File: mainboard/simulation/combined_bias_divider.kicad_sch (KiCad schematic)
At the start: 23 parts

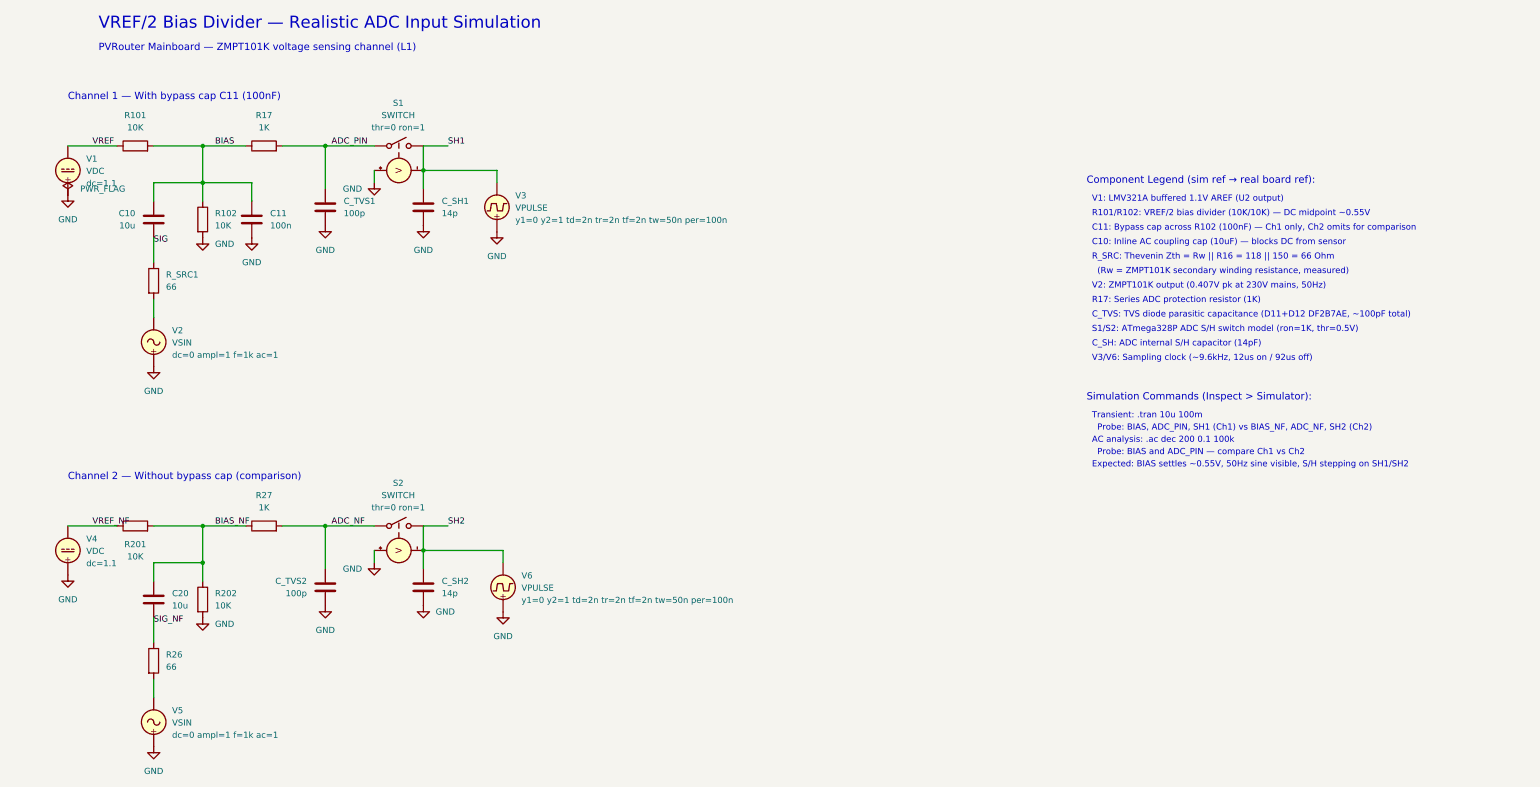
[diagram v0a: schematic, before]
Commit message: Add LCSC part numbers, MPC10-5 footprint, and simulation updates
- Add LCSC fields to mk2Wifi schematic (20 components for JLCPCB assembly)
- Add LCSC fields to mainboard schematic (18x 20K resistors, 12x 100nF caps)
- Add power indicator LED (LED40) and series resistor (R43) to mainboard
- Add MPC10-5 AC-DC converter custom footprint and TMF_05105 3D model
- Add CT and combined bias divider simulation schematics with generators
- Update mainboard PCB layout and bias divider simulation

Co-Authored-By: Claude Opus 4.6 <noreply@anthropic.com>
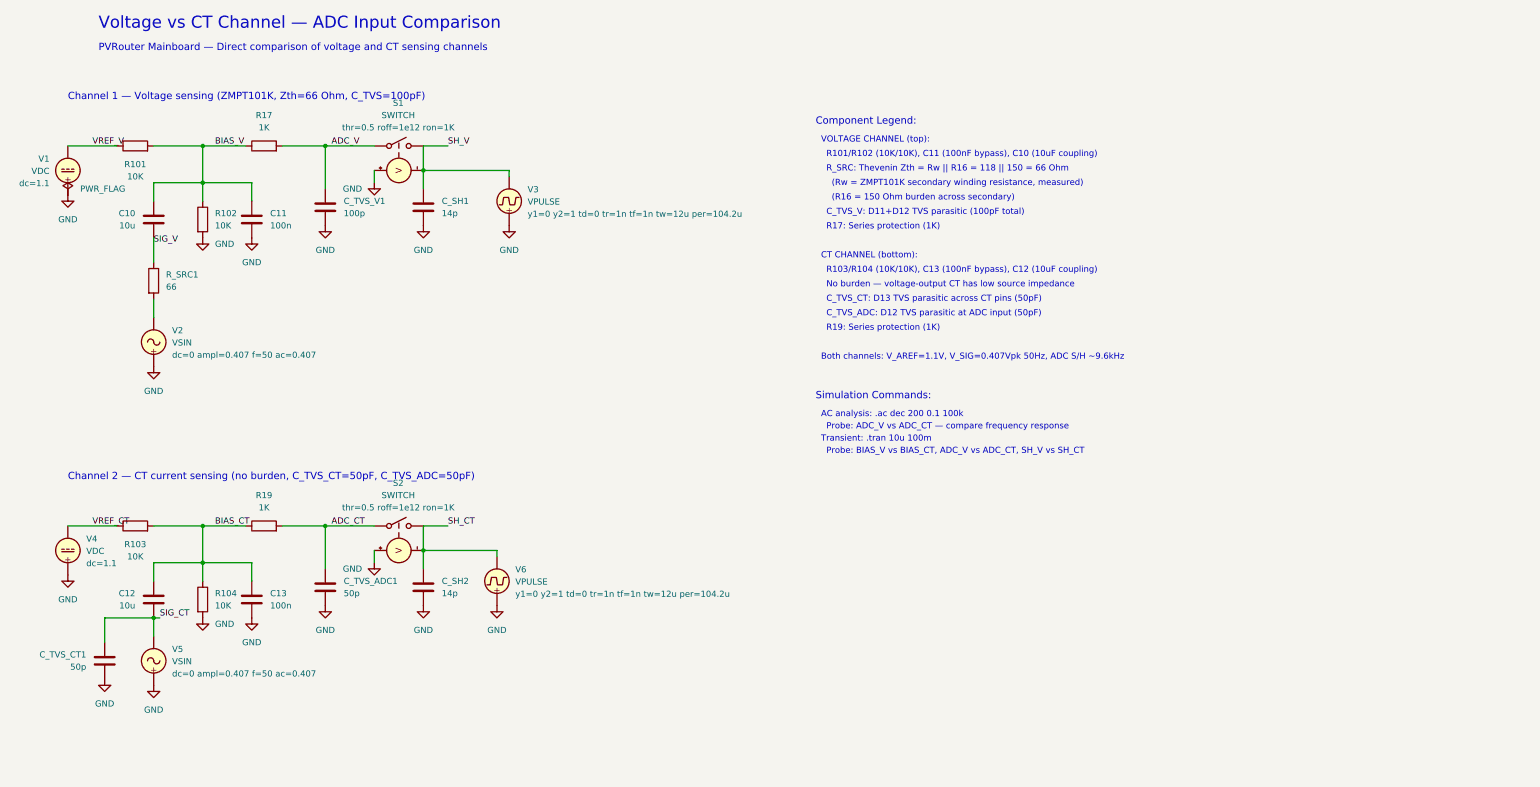
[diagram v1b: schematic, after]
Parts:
- removed C20: 10u, symbol Device:C
- removed C_TVS1, C_TVS2: 100p, symbol Device:C
- removed R201, R202: 10K, symbol Device:R
- removed R26: 66, symbol Device:R
- removed R27: 1K, symbol Device:R
- added C12: 10u, symbol Device:C
- added C13: 100n, symbol Device:C
- added C_TVS_ADC1, C_TVS_CT1: 50p, symbol Device:C
- added C_TVS_V1: 100p, symbol Device:C
- added R103, R104: 10K, symbol Device:R
- added R19: 1K, symbol Device:R
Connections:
- net GND: now also C13.2, C_TVS_ADC1.2, C_TVS_CT1.2, C_TVS_V1.2, R104.2
- net SIG_CT: now reaches V5.2
- net SIG_CT: now also C12.2, C_TVS_CT1.1
- net ADC_NF renamed ADC_CT
- net ADC_CT: now also C_TVS_ADC1.1, R19.2
- net ADC_PIN renamed ADC_V
- net ADC_V: now also C_TVS_V1.1
- net BIAS renamed BIAS_V
- net SH1 renamed SH_V
- net SH2 renamed SH_CT
- net SIG renamed SIG_V
- net VREF renamed VREF_V
- net VREF_NF renamed VREF_CT
- net VREF_CT: now also R103.1
- new net BIAS_CT: C12.1, C13.1, R103.2, R104.1, R19.1
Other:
- note added: "(R16 = 150 Ohm burden across secondary)"
- note added: "Both channels: V_AREF=1.1V, V_SIG=0.407Vpk 50Hz, ADC S/H ~9.6kHz"
- note added: "CT CHANNEL (bottom):"
- note added: "C_TVS_ADC: D12 TVS parasitic at ADC input (50pF)"
- note added: "C_TVS_CT: D13 TVS parasitic across CT pins (50pF)"
- note added: "C_TVS_V: D11+D12 TVS parasitic (100pF total)"
- note added: "Channel 1 — Voltage sensing (ZMPT101K, Zth=66 Ohm, C_TVS=100pF)"
- note added: "Channel 2 — CT current sensing (no burden, C_TVS_CT=50pF, C_TVS_ADC=50pF)"
- note added: "Component Legend:"
- note added: "No burden — voltage-output CT has low source impedance"
- note added: "PVRouter Mainboard — Direct comparison of voltage and CT sensing channels"
- note added: "Probe: ADC_V vs ADC_CT — compare frequency response"
- note added: "Probe: BIAS_V vs BIAS_CT, ADC_V vs ADC_CT, SH_V vs SH_CT"
- note added: "R101/R102 (10K/10K), C11 (100nF bypass), C10 (10uF coupling)"
- note added: "R103/R104 (10K/10K), C13 (100nF bypass), C12 (10uF coupling)"
- note added: "R17: Series protection (1K)"
- note added: "R19: Series protection (1K)"
- note added: "Simulation Commands:"
- note added: "VOLTAGE CHANNEL (top):"
- note added: "Voltage vs CT Channel — ADC Input Comparison"
- note removed: "C10: Inline AC coupling cap (10uF) — blocks DC from sensor"
- note removed: "C11: Bypass cap across R102 (100nF) — Ch1 only, Ch2 omits for comparison"
- note removed: "C_SH: ADC internal S/H capacitor (14pF)"
- note removed: "C_TVS: TVS diode parasitic capacitance (D11+D12 DF2B7AE, ~100pF total)"
- note removed: "Channel 1 — With bypass cap C11 (100nF)"
- note removed: "Channel 2 — Without bypass cap (comparison)"
- note removed: "Component Legend (sim ref → real board ref):"
- note removed: "Expected: BIAS settles ~0.55V, 50Hz sine visible, S/H stepping on SH1/SH2"
- note removed: "PVRouter Mainboard — ZMPT101K voltage sensing channel (L1)"
- note removed: "Probe: BIAS and ADC_PIN — compare Ch1 vs Ch2"
- note removed: "Probe: BIAS, ADC_PIN, SH1 (Ch1) vs BIAS_NF, ADC_NF, SH2 (Ch2)"
- note removed: "R101/R102: VREF/2 bias divider (10K/10K) — DC midpoint ~0.55V"
- note removed: "R17: Series ADC protection resistor (1K)"
- note removed: "S1/S2: ATmega328P ADC S/H switch model (ron=1K, thr=0.5V)"
- note removed: "Simulation Commands (Inspect > Simulator):"
- note removed: "V1: LMV321A buffered 1.1V AREF (U2 output)"
- note removed: "V2: ZMPT101K output (0.407V pk at 230V mains, 50Hz)"
- note removed: "V3/V6: Sampling clock (~9.6kHz, 12us on / 92us off)"
- note removed: "VREF/2 Bias Divider — Realistic ADC Input Simulation"
- title: VREF/2 Bias Divider — Realistic ADC Input Simulation -> Voltage vs CT Channel — ADC Input Comparison
